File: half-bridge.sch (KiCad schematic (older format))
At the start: 16 parts, among them P1 CONN_01X04, P2 CONN_01X02, P3 CONN_01X02, P4 CONN_01X03, Q1 Q_NMOS_GDS, Q2 Q_NMOS_GDS, U1 MOSFET_DRIVER_FAN7842MX

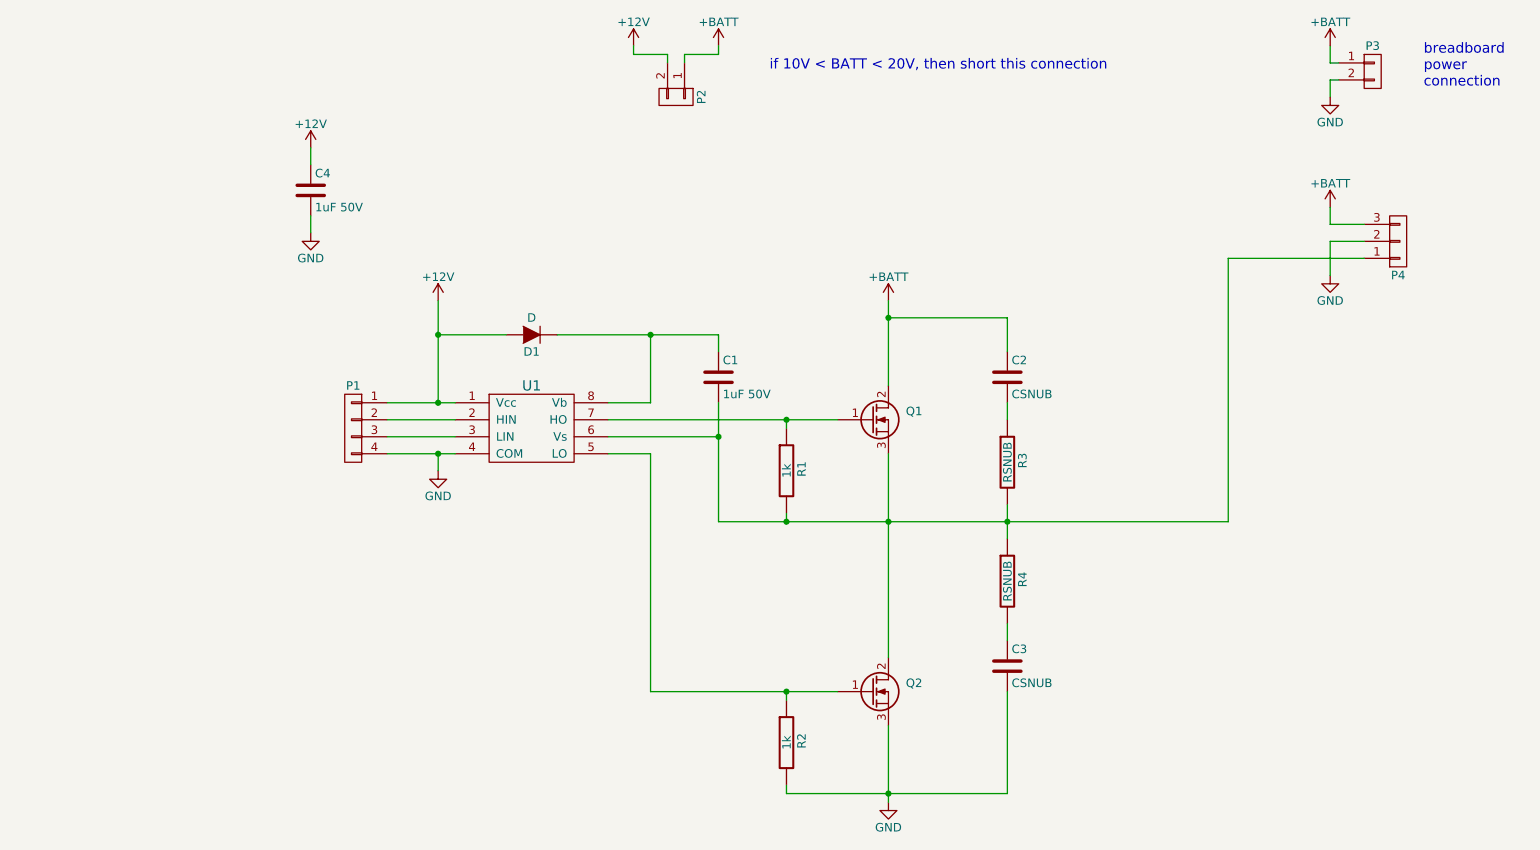
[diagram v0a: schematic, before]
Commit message: Added notes to schematic
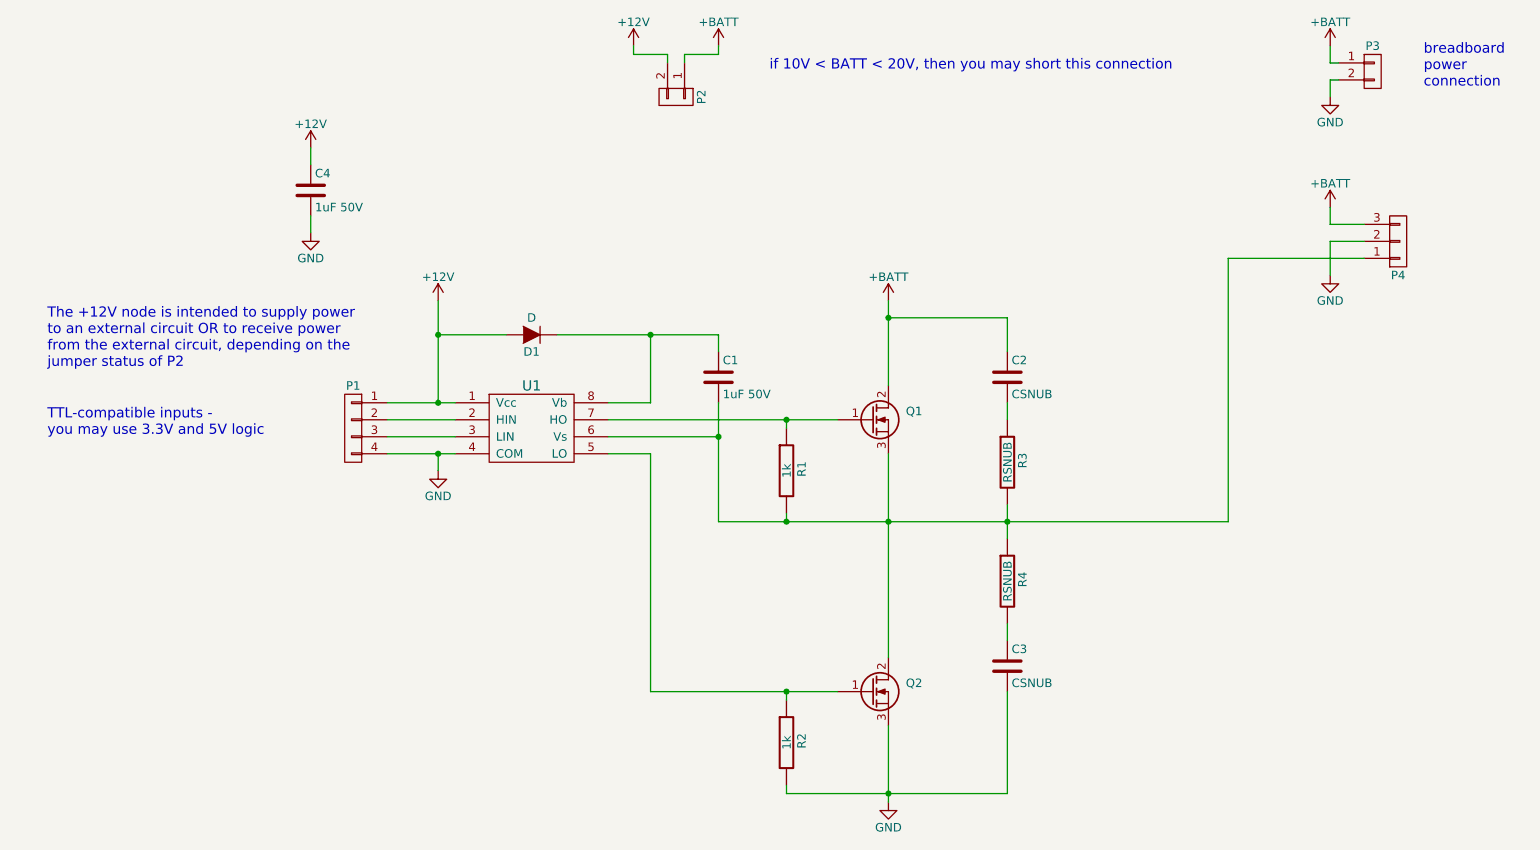
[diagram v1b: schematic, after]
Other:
- note added: "TTL-compatible inputs -\nyou may use 3.3V and 5V logic"
- note added: "The +12V node is intended to supply power\nto an external circuit OR to receive power\nfrom the external circuit, depending on the\njumper status of P2"
- note added: "if 10V < BATT < 20V, then you may short this connection"
- note removed: "if 10V < BATT < 20V, then short this connection"
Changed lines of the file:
@@
 LIBS:contrib
 LIBS:valves
+LIBS:half-bridge-cache
 EELAYER 25 0
 EELAYER END
@@
 encoding utf-8
 Sheet 1 1
-Title ""
-Date ""
-Rev ""
-Comp ""
-Comment1 ""
+Title "half-bridge circuit, breadboard"
+Date "2016-07-14"
+Rev "1.0"
+Comp "for(embed)"
+Comment1 "www.forembed.com"
 Comment2 ""
 Comment3 ""
@@
 breadboard\npower\nconnection
 Text Notes 5000 1150 0    60   ~ 0
-if 10V < BATT < 20V, then short this connection
+if 10V < BATT < 20V, then you may short this connection
 $Comp
 L +12V #PWR011
@@
 Wire Wire Line
 	2300 2000 2300 2100
+Text Notes 750  3300 0    60   ~ 0
+TTL-compatible inputs -\nyou may use 3.3V and 5V logic
+Text Notes 750  2900 0    60   ~ 0
+The +12V node is intended to supply power\nto an external circuit OR to receive power\nfrom the external circuit, depending on the\njumper status of P2
 $EndSCHEMATC

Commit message: Added output sense circuit
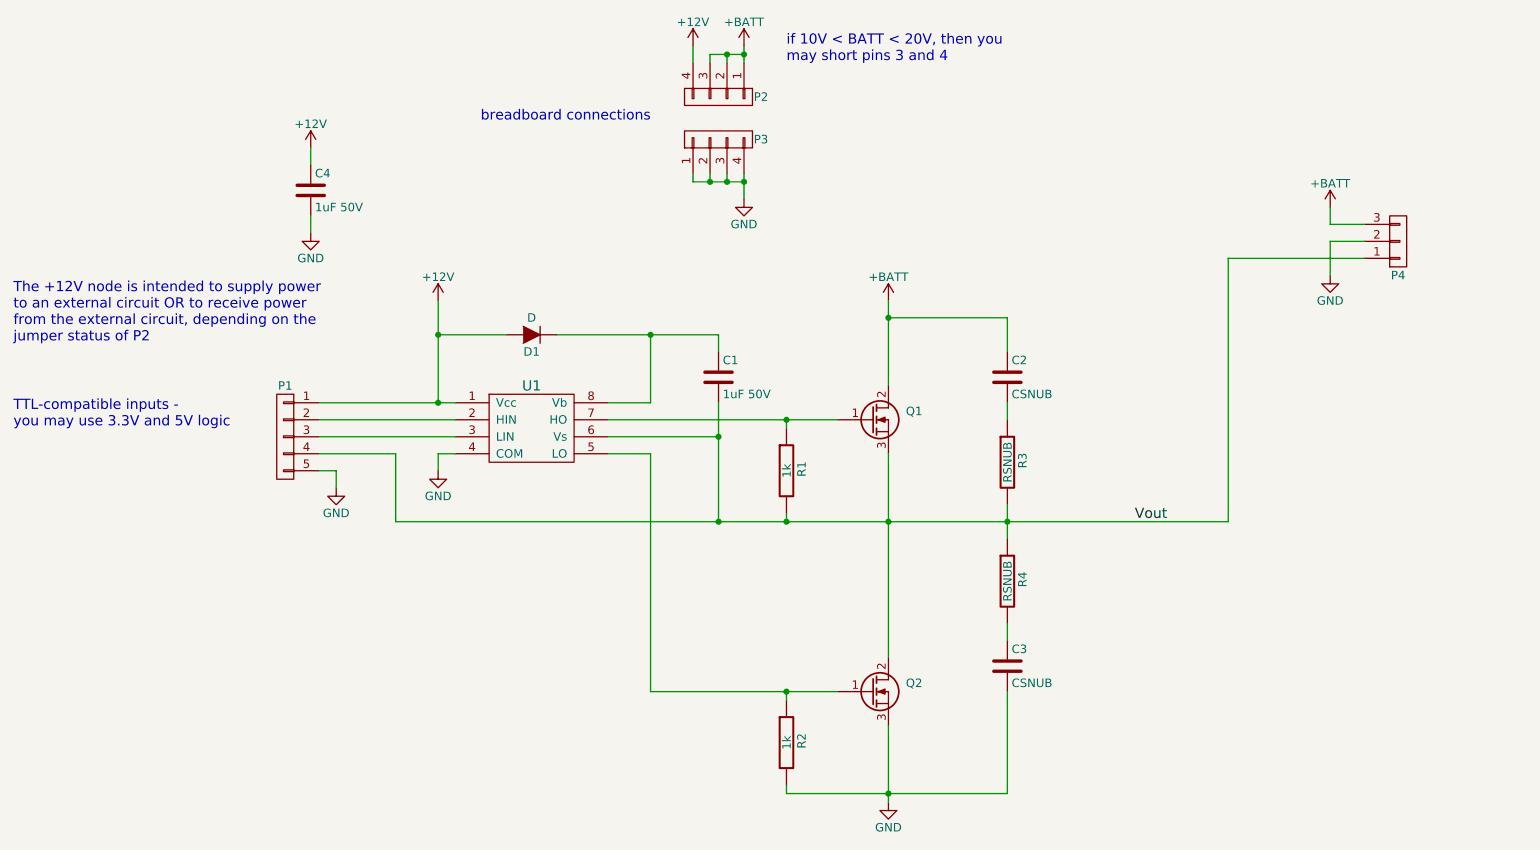
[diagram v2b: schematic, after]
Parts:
- removed P1: CONN_01X04, lib_pcb:CON_1x4_0.1in, symbol CONN_01X04
- removed P2, P3: CONN_01X02, lib_pcb:CON_1x2_0.1in, symbol CONN_01X02
- added P1: CONN_01X05, lib_pcb:CON_1x5_0.1in, symbol CONN_01X05
- added P2, P3: CONN_01X04, lib_pcb:CON_1x4_0.1in, symbol CONN_01X04
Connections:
- net +12V: now also P1.1 (P1), P2.4 (P4)
- net +BATT: now also P2.1 (P1), P2.2 (P2), P2.3 (P3)
- net GND: now also P1.5 (P5), P3.1 (P1), P3.2 (P2), P3.3 (P3), P3.4 (P4)
- net Vout: now reaches C1.2, P4.1 (P1), Q1.3 (S), Q2.2 (D), R1.2, R3.2, R4.1, U1.6 (Vs)
- net Vout: now also P1.4 (P4)
- net at U1.2 (HIN): now also P1.2 (P2)
- net at U1.3 (LIN): now also P1.3 (P3)
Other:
- note added: "breadboard connections"
- note added: "if 10V < BATT < 20V, then you\nmay short pins 3 and 4"
- note removed: "breadboard\npower\nconnection"
- note removed: "if 10V < BATT < 20V, then you may short this connection"
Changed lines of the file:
@@
 $EndComp
 $Comp
-L GND #PWR01
+L GND #PWR10
 U 1 1 5787B49E
 P 5700 5450
-F 0 "#PWR01" H 5700 5200 50  0001 C CNN
+F 0 "#PWR10" H 5700 5200 50  0001 C CNN
 F 1 "GND" H 5700 5300 50  0000 C CNN
 F 2 "" H 5700 5450 50  0000 C CNN
@@
 	5700 5000 5700 5450
 $Comp
-L GND #PWR02
+L GND #PWR5
 U 1 1 5787B712
 P 3050 3500
-F 0 "#PWR02" H 3050 3250 50  0001 C CNN
+F 0 "#PWR5" H 3050 3250 50  0001 C CNN
 F 1 "GND" H 3050 3350 50  0000 C CNN
 F 2 "" H 3050 3500 50  0000 C CNN
@@
 $EndComp
 $Comp
-L +12V #PWR03
+L +12V #PWR4
 U 1 1 5787B735
 P 3050 2500
-F 0 "#PWR03" H 3050 2350 50  0001 C CNN
+F 0 "#PWR4" H 3050 2350 50  0001 C CNN
 F 1 "+12V" H 3050 2640 50  0000 C CNN
 F 2 "" H 3050 2500 50  0000 C CNN
@@
 $EndComp
 $Comp
-L +BATT #PWR04
+L +BATT #PWR9
 U 1 1 5787B74C
 P 5700 2500
-F 0 "#PWR04" H 5700 2350 50  0001 C CNN
+F 0 "#PWR9" H 5700 2350 50  0001 C CNN
 F 1 "+BATT" H 5700 2640 50  0000 C CNN
 F 2 "" H 5700 2500 50  0000 C CNN
@@
 	4700 3100 4700 3800
 Wire Wire Line
-	4700 3800 7700 3800
+	2800 3800 7700 3800
 Connection ~ 5700 3800
 $Comp
@@
 Connection ~ 5700 5400
 $Comp
-L CONN_01X02 P2
-U 1 1 5787BF78
-P 4450 1300
-F 0 "P2" H 4450 1450 50  0000 C CNN
-F 1 "CONN_01X02" V 4550 1300 50  0001 C CNN
-F 2 "lib_pcb:CON_1x2_0.1in" H 4450 1300 50  0001 C CNN
-F 3 "" H 4450 1300 50  0000 C CNN
-	1    4450 1300
-	0    1    1    0
-$EndComp
-$Comp
-L +BATT #PWR05
+L +BATT #PWR7
 U 1 1 5787C032
-P 4700 1000
-F 0 "#PWR05" H 4700 850 50  0001 C CNN
-F 1 "+BATT" H 4700 1140 50  0000 C CNN
-F 2 "" H 4700 1000 50  0000 C CNN
-F 3 "" H 4700 1000 50  0000 C CNN
-	1    4700 1000
-	1    0    0    -1
-$EndComp
-$Comp
-L +12V #PWR06
+P 4850 1000
+F 0 "#PWR7" H 4850 850 50  0001 C CNN
+F 1 "+BATT" H 4850 1140 50  0000 C CNN
+F 2 "" H 4850 1000 50  0000 C CNN
+F 3 "" H 4850 1000 50  0000 C CNN
+	1    4850 1000
+	1    0    0    -1
+$EndComp
+$Comp
+L +12V #PWR6
 U 1 1 5787C052
-P 4200 1000
-F 0 "#PWR06" H 4200 850 50  0001 C CNN
-F 1 "+12V" H 4200 1140 50  0000 C CNN
-F 2 "" H 4200 1000 50  0000 C CNN
-F 3 "" H 4200 1000 50  0000 C CNN
-	1    4200 1000
-	1    0    0    -1
-$EndComp
-Wire Wire Line
-	4500 1100 4500 1050
-Wire Wire Line
-	4500 1050 4700 1050
-Wire Wire Line
-	4700 1050 4700 1000
-Wire Wire Line
-	4400 1100 4400 1050
-Wire Wire Line
-	4400 1050 4200 1050
-Wire Wire Line
-	4200 1050 4200 1000
-Wire Wire Line
-	2750 3400 3150 3400
+P 4550 1000
+F 0 "#PWR6" H 4550 850 50  0001 C CNN
+F 1 "+12V" H 4550 1140 50  0000 C CNN
+F 2 "" H 4550 1000 50  0000 C CNN
+F 3 "" H 4550 1000 50  0000 C CNN
+	1    4550 1000
+	1    0    0    -1
+$EndComp
+Wire Wire Line
+	3050 3400 3150 3400
 Wire Wire Line
 	3050 3400 3050 3500
 Wire Wire Line
-	2750 3100 3150 3100
+	2350 3100 3150 3100
 Wire Wire Line
 	3050 2500 3050 3100
@@
 	6400 2600 5700 2600
 Connection ~ 5700 2600
-$Comp
-L CONN_01X04 P1
-U 1 1 5787D2E2
-P 2550 3250
-F 0 "P1" H 2550 3500 50  0000 C CNN
-F 1 "CONN_01X04" V 2650 3250 50  0001 C CNN
-F 2 "lib_pcb:CON_1x4_0.1in" H 2550 3250 50  0001 C CNN
-F 3 "" H 2550 3250 50  0000 C CNN
-	1    2550 3250
-	-1   0    0    -1
-$EndComp
 Connection ~ 3050 3100
 Wire Wire Line
-	2750 3200 3150 3200
-Wire Wire Line
-	2750 3300 3150 3300
-Connection ~ 3050 3400
+	2350 3200 3150 3200
+Wire Wire Line
+	2350 3300 3150 3300
 $Comp
 L CONN_01X03 P4
@@
 $EndComp
 $Comp
-L +BATT #PWR07
+L +BATT #PWR11
 U 1 1 5787D95E
 P 8300 1950
-F 0 "#PWR07" H 8300 1800 50  0001 C CNN
+F 0 "#PWR11" H 8300 1800 50  0001 C CNN
 F 1 "+BATT" H 8300 2090 50  0000 C CNN
 F 2 "" H 8300 1950 50  0000 C CNN
@@
 	7700 2250 7700 3800
 $Comp
-L CONN_01X02 P3
-U 1 1 5787E1AA
-P 8550 1150
-F 0 "P3" H 8550 1300 50  0000 C CNN
-F 1 "CONN_01X02" V 8650 1150 50  0001 C CNN
-F 2 "lib_pcb:CON_1x2_0.1in" H 8550 1150 50  0001 C CNN
-F 3 "" H 8550 1150 50  0000 C CNN
-	1    8550 1150
-	1    0    0    -1
-$EndComp
-Wire Wire Line
-	8350 1100 8300 1100
-Wire Wire Line
-	8300 1100 8300 1000
-Wire Wire Line
-	8350 1200 8300 1200
-Wire Wire Line
-	8300 1200 8300 1300
-$Comp
-L GND #PWR08
+L GND #PWR12
 U 1 1 5787D993
 P 8300 2350
-F 0 "#PWR08" H 8300 2100 50  0001 C CNN
+F 0 "#PWR12" H 8300 2100 50  0001 C CNN
 F 1 "GND" H 8300 2200 50  0000 C CNN
 F 2 "" H 8300 2350 50  0000 C CNN
@@
 $EndComp
 $Comp
-L +BATT #PWR09
-U 1 1 5787E85D
-P 8300 1000
-F 0 "#PWR09" H 8300 850 50  0001 C CNN
-F 1 "+BATT" H 8300 1140 50  0000 C CNN
-F 2 "" H 8300 1000 50  0000 C CNN
-F 3 "" H 8300 1000 50  0000 C CNN
-	1    8300 1000
-	1    0    0    -1
-$EndComp
-$Comp
-L GND #PWR010
+L GND #PWR8
 U 1 1 5787E895
-P 8300 1300
-F 0 "#PWR010" H 8300 1050 50  0001 C CNN
-F 1 "GND" H 8300 1150 50  0000 C CNN
-F 2 "" H 8300 1300 50  0000 C CNN
-F 3 "" H 8300 1300 50  0000 C CNN
-	1    8300 1300
-	1    0    0    -1
-$EndComp
-Text Notes 8850 1250 0    60   ~ 0
-breadboard\npower\nconnection
-Text Notes 5000 1150 0    60   ~ 0
-if 10V < BATT < 20V, then you may short this connection
-$Comp
-L +12V #PWR011
+P 4850 1900
+F 0 "#PWR8" H 4850 1650 50  0001 C CNN
+F 1 "GND" H 4850 1750 50  0000 C CNN
+F 2 "" H 4850 1900 50  0000 C CNN
+F 3 "" H 4850 1900 50  0000 C CNN
+	1    4850 1900
+	1    0    0    -1
+$EndComp
+Text Notes 5100 1100 0    60   ~ 0
+if 10V < BATT < 20V, then you\nmay short pins 3 and 4
+$Comp
+L +12V #PWR1
 U 1 1 5787FC0F
 P 2300 1600
-F 0 "#PWR011" H 2300 1450 50  0001 C CNN
+F 0 "#PWR1" H 2300 1450 50  0001 C CNN
 F 1 "+12V" H 2300 1740 50  0000 C CNN
 F 2 "" H 2300 1600 50  0000 C CNN
@@
 $EndComp
 $Comp
-L GND #PWR012
+L GND #PWR2
 U 1 1 5787FCF5
 P 2300 2100
-F 0 "#PWR012" H 2300 1850 50  0001 C CNN
+F 0 "#PWR2" H 2300 1850 50  0001 C CNN
 F 1 "GND" H 2300 1950 50  0000 C CNN
 F 2 "" H 2300 2100 50  0000 C CNN
@@
 Wire Wire Line
 	2300 2000 2300 2100
-Text Notes 750  3300 0    60   ~ 0
+Text Notes 550  3250 0    60   ~ 0
 TTL-compatible inputs -\nyou may use 3.3V and 5V logic
-Text Notes 750  2900 0    60   ~ 0
+Text Notes 550  2750 0    60   ~ 0
 The +12V node is intended to supply power\nto an external circuit OR to receive power\nfrom the external circuit, depending on the\njumper status of P2
+Wire Wire Line
+	4850 1000 4850 1100
+Wire Wire Line
+	4650 1050 4850 1050
+Wire Wire Line
+	4750 1050 4750 1100
+Wire Wire Line
+	4650 1100 4650 1050
+Connection ~ 4750 1050
+Wire Wire Line
+	4550 1000 4550 1100
+$Comp
+L CONN_01X04 P2
+U 1 1 578800C5
+P 4700 1300
+F 0 "P2" V 4700 1550 50  0000 C CNN
+F 1 "CONN_01X04" V 4800 1300 50  0001 C CNN
+F 2 "lib_pcb:CON_1x4_0.1in" H 4700 1300 50  0001 C CNN
+F 3 "" H 4700 1300 50  0000 C CNN
+	1    4700 1300
+	0    1    1    0
+$EndComp
+Connection ~ 4850 1050
+$Comp
+L CONN_01X04 P3
+U 1 1 57880949
+P 4700 1550
+F 0 "P3" V 4700 1300 50  0000 C CNN
+F 1 "CONN_01X04" V 4800 1550 50  0001 C CNN
+F 2 "lib_pcb:CON_1x4_0.1in" H 4700 1550 50  0001 C CNN
+F 3 "" H 4700 1550 50  0000 C CNN
+	1    4700 1550
+	0    -1   -1   0
+$EndComp
+Wire Wire Line
+	4850 1750 4850 1900
+Wire Wire Line
+	4550 1800 4850 1800
+Wire Wire Line
+	4750 1800 4750 1750
+Connection ~ 4850 1800
+Wire Wire Line
+	4650 1750 4650 1800
+Connection ~ 4750 1800
+Wire Wire Line
+	4550 1750 4550 1800
+Connection ~ 4650 1800
+Text Notes 3300 1450 0    60   ~ 0
+breadboard connections
+$Comp
+L CONN_01X05 P1
+U 1 1 578826C0
+P 2150 3300
+F 0 "P1" H 2150 3600 50  0000 C CNN
+F 1 "CONN_01X05" V 2250 3300 50  0001 C CNN
+F 2 "lib_pcb:CON_1x5_0.1in" H 2150 3300 50  0001 C CNN
+F 3 "" H 2150 3300 50  0000 C CNN
+	1    2150 3300
+	-1   0    0    -1
+$EndComp
+$Comp
+L GND #PWR3
+U 1 1 57882A41
+P 2450 3600
+F 0 "#PWR3" H 2450 3350 50  0001 C CNN
+F 1 "GND" H 2450 3450 50  0000 C CNN
+F 2 "" H 2450 3600 50  0000 C CNN
+F 3 "" H 2450 3600 50  0000 C CNN
+	1    2450 3600
+	1    0    0    -1
+$EndComp
+Wire Wire Line
+	2800 3800 2800 3400
+Wire Wire Line
+	2800 3400 2350 3400
+Connection ~ 4700 3800
+Wire Wire Line
+	2350 3500 2450 3500
+Wire Wire Line
+	2450 3500 2450 3600
+Text Label 7150 3800 0    60   ~ 0
+Vout
 $EndSCHEMATC
